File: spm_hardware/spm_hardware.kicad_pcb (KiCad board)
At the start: 2 copper layers, 29 parts, among them J1 Magnet sensor, J2 Floater, J3 MotIn, J4 MotOut, J5 230VAC, J6 USonic sensor, J7 Temp&Humid sensor, J8 Flow sensor, J9 HAL sensor, P1 DIL16, Q1 BS170, T1 Transformer_1P_1S

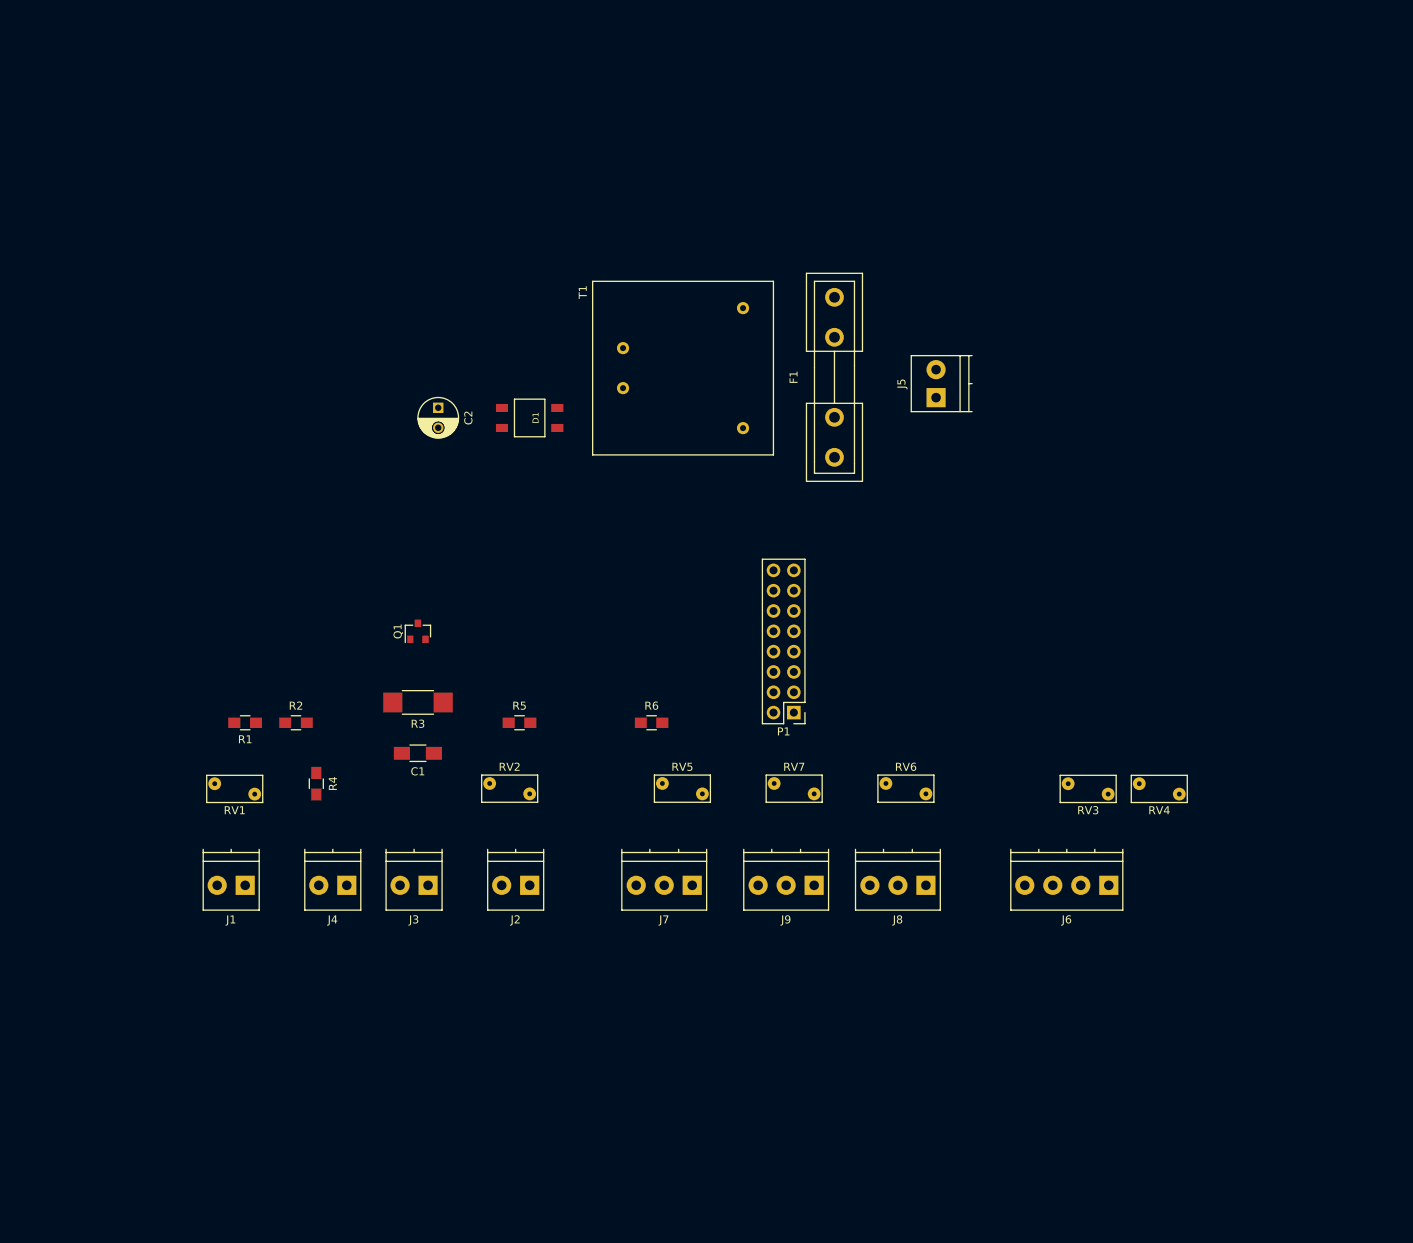
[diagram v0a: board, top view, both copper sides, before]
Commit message: Create PCB sketch
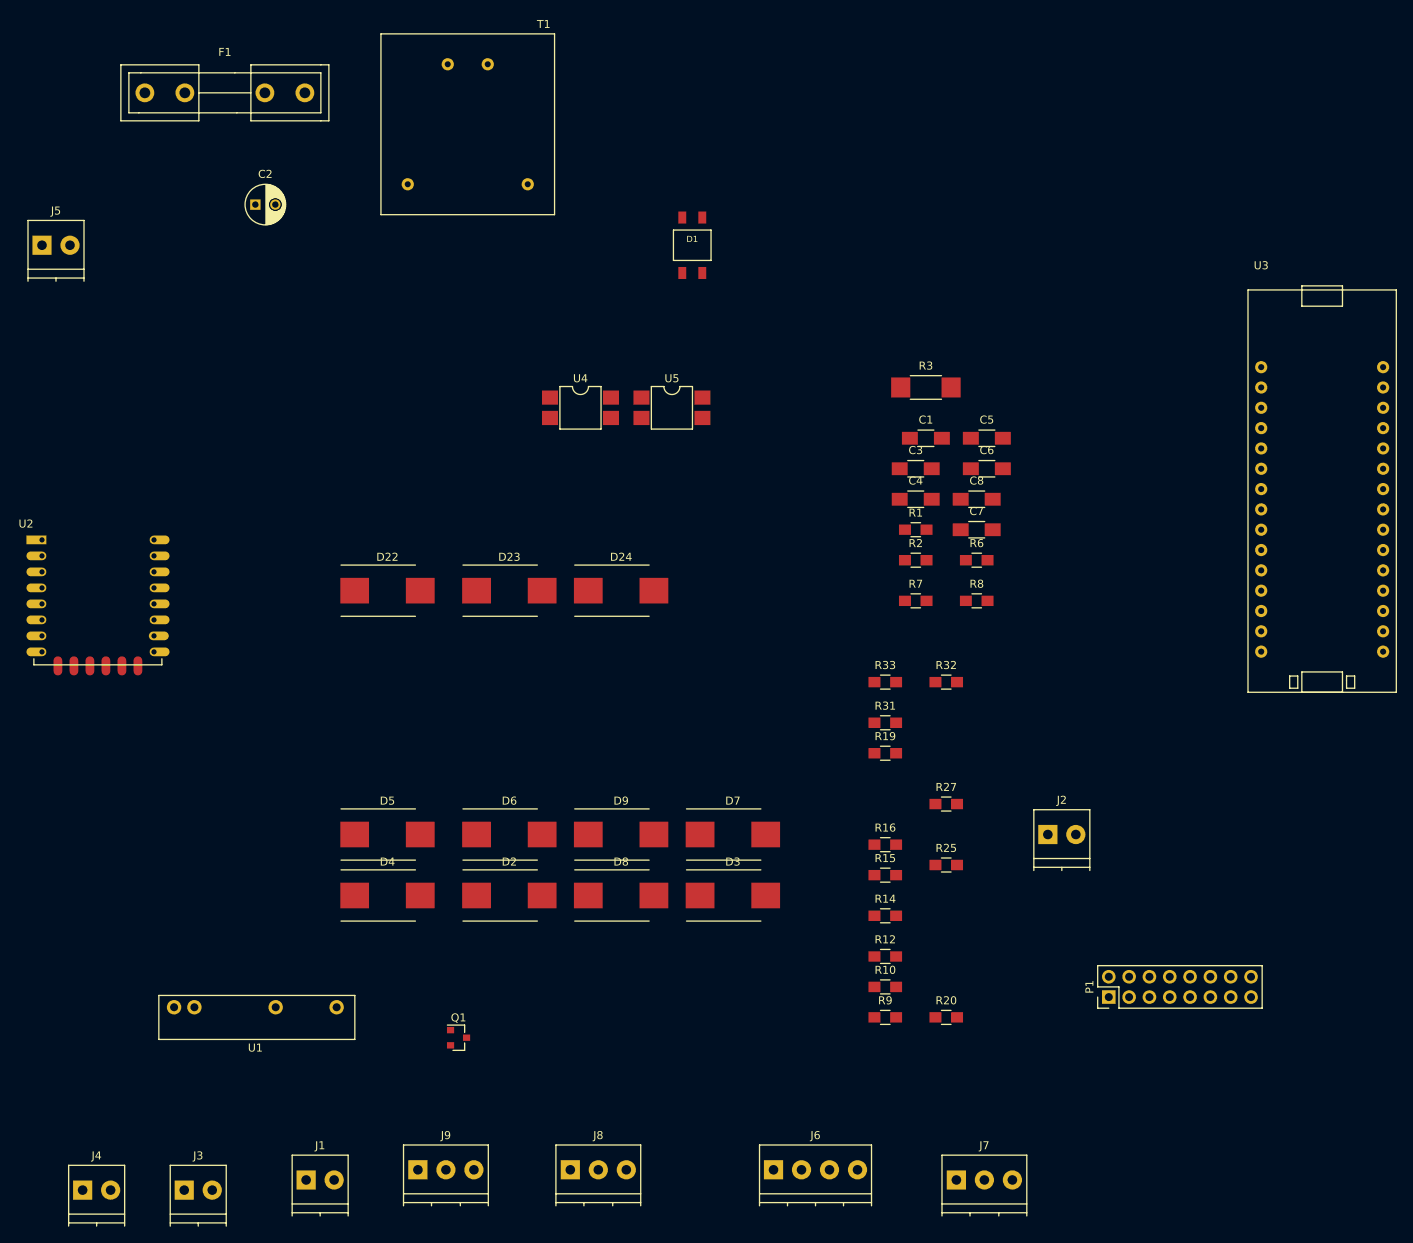
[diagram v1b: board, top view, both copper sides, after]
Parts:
- removed R4, R5: R, Resistors_SMD:R_0805_HandSoldering
- removed RV1, RV2, RV3, RV4, RV5, RV6, RV7: Varistor, Varistors:RV_Disc_D7_W3.4_P5
- added C3: C, Capacitors_SMD:C_1206_HandSoldering, F.Cu at (151.1, 78.7)
- added C4: C, Capacitors_SMD:C_1206_HandSoldering, F.Cu at (151.1, 82.5)
- added C5: C, Capacitors_SMD:C_1206_HandSoldering, F.Cu at (160.0, 74.9)
- added C6: C, Capacitors_SMD:C_1206_HandSoldering, F.Cu at (160.0, 78.7)
- added C7: C, Capacitors_SMD:C_1206_HandSoldering, F.Cu at (158.8, 86.4)
- added C8: C, Capacitors_SMD:C_1206_HandSoldering, F.Cu at (158.8, 82.5)
- added D2: D_TVS, Diodes_SMD:DO-214AB_Handsoldering, F.Cu at (100.3, 132.1)
- added D22: D_TVS, Diodes_SMD:DO-214AB_Handsoldering, F.Cu at (85.1, 94.0)
- added D23: D_TVS, Diodes_SMD:DO-214AB_Handsoldering, F.Cu at (100.3, 94.0)
- added D24: D_TVS, Diodes_SMD:DO-214AB_Handsoldering, F.Cu at (114.3, 94.0)
- added D3: D_TVS, Diodes_SMD:DO-214AB_Handsoldering, F.Cu at (128.3, 132.1)
- added D4: D_TVS, Diodes_SMD:DO-214AB_Handsoldering, F.Cu at (85.1, 132.1)
- added D5: D_Zener, Diodes_SMD:DO-214AB_Handsoldering, F.Cu at (85.1, 124.5)
- added D6: D_TVS, Diodes_SMD:DO-214AB_Handsoldering, F.Cu at (100.3, 124.5)
- added D7: D_TVS, Diodes_SMD:DO-214AB_Handsoldering, F.Cu at (128.3, 124.5)
- added D8: D_TVS, Diodes_SMD:DO-214AB_Handsoldering, F.Cu at (114.3, 132.1)
- added D9: D_TVS, Diodes_SMD:DO-214AB_Handsoldering, F.Cu at (114.3, 124.5)
- added R10: R, Resistors_SMD:R_0805_HandSoldering, F.Cu at (147.3, 143.5)
- added R12: R, Resistors_SMD:R_0805_HandSoldering, F.Cu at (147.3, 139.7)
- added R14: R, Resistors_SMD:R_0805_HandSoldering, F.Cu at (147.3, 134.6)
- added R15: R, Resistors_SMD:R_0805_HandSoldering, F.Cu at (147.3, 129.5)
- added R16: R, Resistors_SMD:R_0805_HandSoldering, F.Cu at (147.3, 125.7)
- added R19: R, Resistors_SMD:R_0805_HandSoldering, F.Cu at (147.3, 114.3)
- added R20: R, Resistors_SMD:R_0805_HandSoldering, F.Cu at (154.9, 147.3)
- added R25: R, Resistors_SMD:R_0805_HandSoldering, F.Cu at (154.9, 128.3)
- added R27: R, Resistors_SMD:R_0805_HandSoldering, F.Cu at (154.9, 120.7)
- added R31: R, Resistors_SMD:R_0805_HandSoldering, F.Cu at (147.3, 110.5)
- added R32: R, Resistors_SMD:R_0805_HandSoldering, F.Cu at (154.9, 105.4)
- added R33: R, Resistors_SMD:R_0805_HandSoldering, F.Cu at (147.3, 105.4)
- added R7: R, Resistors_SMD:R_0805_HandSoldering, F.Cu at (151.1, 95.2)
- added R8: R, Resistors_SMD:R_0805_HandSoldering, F.Cu at (158.8, 95.2)
- added R9: R, Resistors_SMD:R_0805_HandSoldering, F.Cu at (147.3, 147.3)
- added U1: G3MB-202P, G3MB-202P:G3MB-202P, F.Cu at (58.4, 146.1)
- added U2: ESP-12E, ESP8266:ESP-12E, F.Cu at (41.9, 87.6)
- added U3: STM32L432, STM32L432:STM32L432, F.Cu at (194.3, 101.6)
- added U4: LTV-817, Housings_DIP:DIP-4_W7.62mm_SMD, F.Cu at (109.2, 71.1)
- added U5: LTV-817, Housings_DIP:DIP-4_W7.62mm_SMD, F.Cu at (120.7, 71.1)
- moved J5 113.4 mm to (41.9, 50.8), turned to 0 degrees
- moved R1 87.2 mm to (151.1, 86.4), turned to 0 degrees
- moved F1 84.1 mm to (64.8, 31.8), turned to 0 degrees
- moved R2 80.1 mm to (151.1, 90.2)
- moved R3 74.7 mm to (152.4, 68.6), turned to 0 degrees
- moved C1 74.7 mm to (152.4, 74.9), turned to 0 degrees
- moved J2 65.1 mm to (167.6, 124.5), turned to 0 degrees
- moved J9 61.0 mm to (88.9, 166.4), turned to 0 degrees
- moved J8 56.9 mm to (108.0, 166.4), turned to 0 degrees
- moved J6 55.0 mm to (133.3, 166.4), turned to 0 degrees
- moved P1 53.1 mm to (175.3, 144.8), turned to 90 degrees
- moved T1 51.8 mm to (87.6, 43.2), turned to 0 degrees
- moved Q1 51.1 mm to (94.0, 149.9), turned to 0 degrees
- moved J4 50.4 mm to (47.0, 168.9), turned to 0 degrees
- moved J7 49.5 mm to (156.2, 167.6), turned to 0 degrees
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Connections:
- J1 pad 1: Net-(J1-Pad1) -> +5V
- J1 pad 2: Mag_Sw -> Net-(D2-Pad1)
- J2 pad 1: Net-(J2-Pad1) -> +5V
- J2 pad 2: Floater -> Net-(D3-Pad1)
- J6 pad 2: USonic_trigger -> Net-(D23-Pad1)
- J6 pad 3: USonic_echo -> Net-(D22-Pad2)
- J7 pad 2: TH_Sensor -> Net-(J7-Pad2)
- J8 pad 2: Flow_Sen -> Net-(D4-Pad1)
- J9 pad 2: HAL_Sen -> Net-(C3-Pad1)
- P1 pad 10: PA1/ADC12_IN6 -> PA0/ADC12_IN5
- P1 pad 11: PA0/ADC12_IN5 -> PA1/ADC12_IN6
- Q1 pad 2: MOT_Off -> Net-(Q1-Pad2)
- R1 pad 1: +3V3 -> Net-(R1-Pad1)
- R1 pad 2: Net-(J1-Pad1) -> GND
- R2 pad 1: +3V3 -> Mag_Sw
- R2 pad 2: Net-(J2-Pad1) -> Net-(R1-Pad1)
